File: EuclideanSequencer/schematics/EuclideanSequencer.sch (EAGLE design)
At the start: 46 parts, among them IC1 MEGA168, Q1 2N3904, Q2 2N3904, Q3 2N3904, Q4 2N3904, Y1 16Mhz

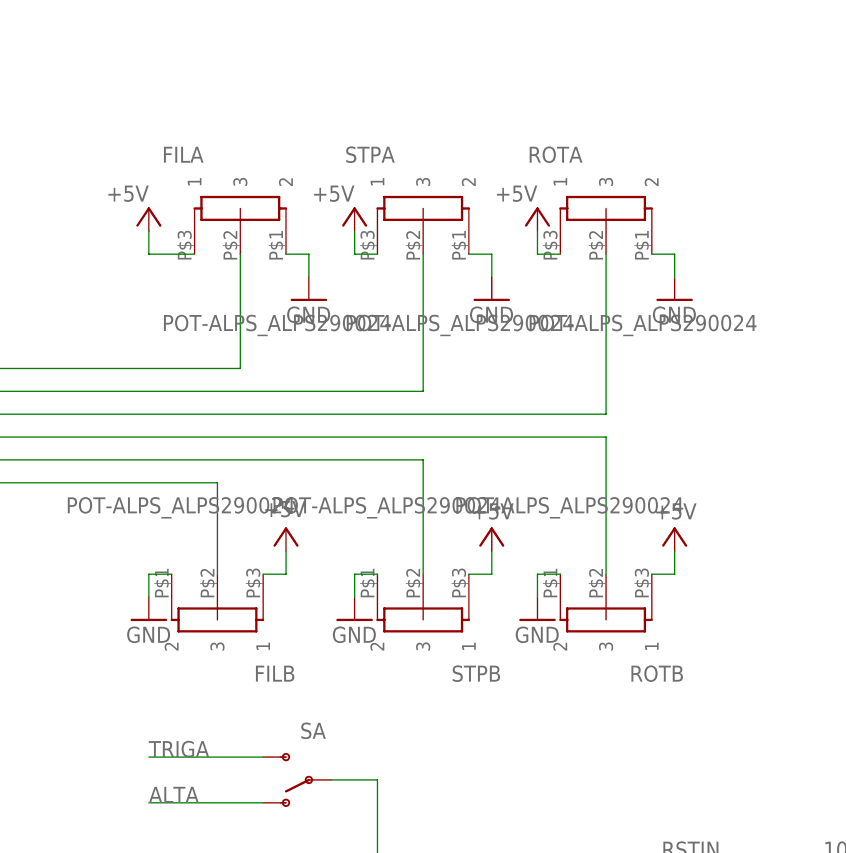
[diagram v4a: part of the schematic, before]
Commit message: moved pots around.
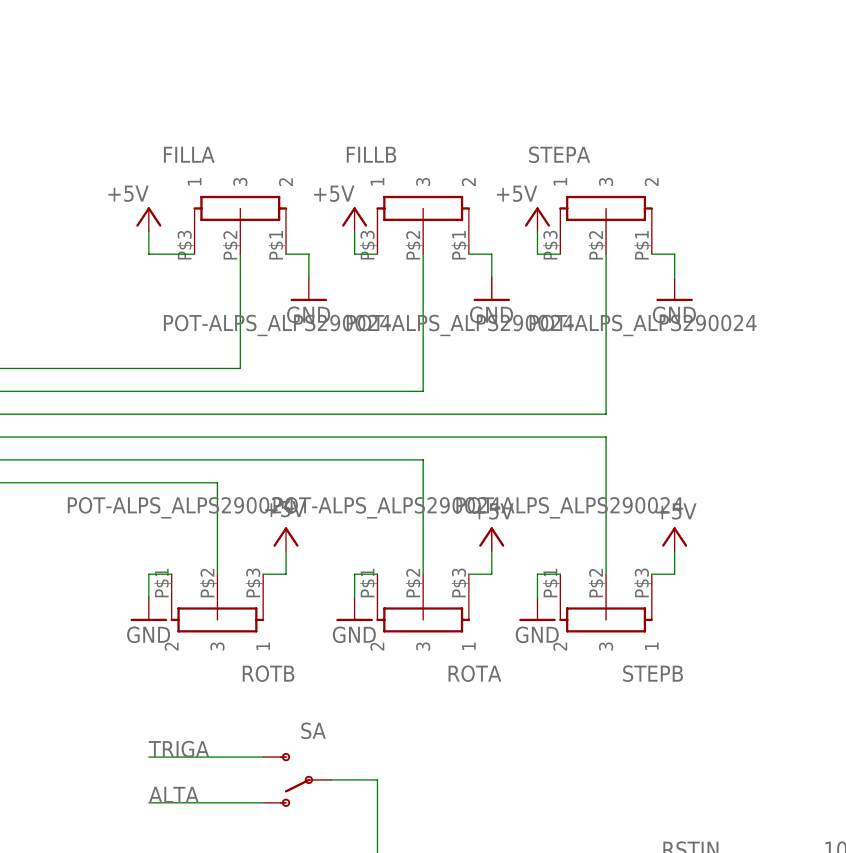
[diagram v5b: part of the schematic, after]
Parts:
- removed FILB, STPB: POT-ALPS_ALPS290024, Rebel:POT-ALPS_ALPS290024
- added STEPA, STEPB: POT-ALPS_ALPS290024, Rebel:POT-ALPS_ALPS290024
- renumbered FILA to FILLA, STPA to FILLB
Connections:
- net N$2 renamed FILFB
- net +5V: now also STEPA.1, STEPB.1; no longer FILB.1, STPB.1
- net GND: now also STEPA.2, STEPB.2; no longer FILB.2, STPB.2
- net N$3: now also STEPA.3; no longer ROTA.3
- net N$4: now also STEPB.3; no longer ROTB.3
- net N$5: now also ROTA.3; no longer STPB.3
- net N$6: now also ROTB.3; no longer FILB.3
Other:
- moved on the sheet: ROTA, ROTB
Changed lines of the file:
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@@
 <part name="CLKB" library="Rebel" deviceset="CON-LUMBERG_1502_03" device=""/>
 <part name="CLKTH" library="Rebel" deviceset="CON-LUMBERG_1502_03" device=""/>
-<part name="FILA" library="Rebel" deviceset="POT-ALPS_ALPS290024" device=""/>
-<part name="STPA" library="Rebel" deviceset="POT-ALPS_ALPS290024" device=""/>
+<part name="FILLA" library="Rebel" deviceset="POT-ALPS_ALPS290024" device=""/>
+<part name="FILLB" library="Rebel" deviceset="POT-ALPS_ALPS290024" device=""/>
+<part name="STEPA" library="Rebel" deviceset="POT-ALPS_ALPS290024" device=""/>
+<part name="ROTB" library="Rebel" deviceset="POT-ALPS_ALPS290024" device=""/>
 <part name="ROTA" library="Rebel" deviceset="POT-ALPS_ALPS290024" device=""/>
-<part name="FILB" library="Rebel" deviceset="POT-ALPS_ALPS290024" device=""/>
-<part name="STPB" library="Rebel" deviceset="POT-ALPS_ALPS290024" device=""/>
-<part name="ROTB" library="Rebel" deviceset="POT-ALPS_ALPS290024" device=""/>
+<part name="STEPB" library="Rebel" deviceset="POT-ALPS_ALPS290024" device=""/>
 <part name="CLKIN" library="Rebel" deviceset="CON-LUMBERG_1502_03" device=""/>
 <part name="RSTIN" library="Rebel" deviceset="CON-LUMBERG_1502_03" device=""/>
@@
 <instance part="CLKB" gate="G$1" x="144.78" y="-35.56"/>
 <instance part="CLKTH" gate="G$1" x="-7.62" y="-20.32" rot="MR0"/>
-<instance part="FILA" gate="G$1" x="139.7" y="91.44"/>
-<instance part="STPA" gate="G$1" x="160.02" y="91.44"/>
-<instance part="ROTA" gate="G$1" x="180.34" y="91.44"/>
-<instance part="FILB" gate="G$1" x="137.16" y="45.72" rot="R180"/>
-<instance part="STPB" gate="G$1" x="160.02" y="45.72" rot="R180"/>
-<instance part="ROTB" gate="G$1" x="180.34" y="45.72" rot="R180"/>
+<instance part="FILLA" gate="G$1" x="139.7" y="91.44"/>
+<instance part="FILLB" gate="G$1" x="160.02" y="91.44"/>
+<instance part="STEPA" gate="G$1" x="180.34" y="91.44"/>
+<instance part="ROTB" gate="G$1" x="137.16" y="45.72" rot="R180"/>
+<instance part="ROTA" gate="G$1" x="160.02" y="45.72" rot="R180"/>
+<instance part="STEPB" gate="G$1" x="180.34" y="45.72" rot="R180"/>
 <instance part="CLKIN" gate="G$1" x="-7.62" y="-43.18" rot="MR0"/>
 <instance part="RSTIN" gate="G$1" x="190.5" y="15.24" rot="MR0"/>
@@
 <wire x1="81.28" y1="73.66" x2="139.7" y2="73.66" width="0.1524" layer="91"/>
 <wire x1="139.7" y1="73.66" x2="139.7" y2="86.36" width="0.1524" layer="91"/>
-<pinref part="FILA" gate="G$1" pin="3"/>
-</segment>
-</net>
-<net name="N$2" class="0">
+<pinref part="FILLA" gate="G$1" pin="3"/>
+</segment>
+</net>
+<net name="FILFB" class="0">
 <segment>
 <pinref part="IC1" gate="G$1" pin="PC1(ADC1)"/>
 <wire x1="81.28" y1="71.12" x2="160.02" y2="71.12" width="0.1524" layer="91"/>
 <wire x1="160.02" y1="71.12" x2="160.02" y2="86.36" width="0.1524" layer="91"/>
-<pinref part="STPA" gate="G$1" pin="3"/>
+<pinref part="FILLB" gate="G$1" pin="3"/>
 </segment>
 </net>
@@
 <wire x1="81.28" y1="68.58" x2="180.34" y2="68.58" width="0.1524" layer="91"/>
 <wire x1="180.34" y1="68.58" x2="180.34" y2="86.36" width="0.1524" layer="91"/>
-<pinref part="ROTA" gate="G$1" pin="3"/>
+<pinref part="STEPA" gate="G$1" pin="3"/>
 </segment>
 </net>
@@
 <wire x1="81.28" y1="66.04" x2="180.34" y2="66.04" width="0.1524" layer="91"/>
 <wire x1="180.34" y1="66.04" x2="180.34" y2="50.8" width="0.1524" layer="91"/>
-<pinref part="ROTB" gate="G$1" pin="3"/>
+<pinref part="STEPB" gate="G$1" pin="3"/>
 </segment>
 </net>
@@
 <wire x1="81.28" y1="63.5" x2="160.02" y2="63.5" width="0.1524" layer="91"/>
 <wire x1="160.02" y1="63.5" x2="160.02" y2="50.8" width="0.1524" layer="91"/>
-<pinref part="STPB" gate="G$1" pin="3"/>
+<pinref part="ROTA" gate="G$1" pin="3"/>
 </segment>
 </net>
@@
 <pinref part="IC1" gate="G$1" pin="PC5(ADC5/SCL)"/>
 <wire x1="81.28" y1="60.96" x2="137.16" y2="60.96" width="0.1524" layer="91"/>
-<pinref part="FILB" gate="G$1" pin="3"/>
+<pinref part="ROTB" gate="G$1" pin="3"/>
 <wire x1="137.16" y1="50.8" x2="137.16" y2="60.96" width="0.1524" layer="91"/>
 </segment>
@@
 <pinref part="P+1" gate="1" pin="+5V"/>
 <wire x1="129.54" y1="88.9" x2="129.54" y2="86.36" width="0.1524" layer="91"/>
-<pinref part="FILA" gate="G$1" pin="1"/>
+<pinref part="FILLA" gate="G$1" pin="1"/>
 <wire x1="129.54" y1="86.36" x2="134.62" y2="86.36" width="0.1524" layer="91"/>
 </segment>
@@
 <pinref part="P+2" gate="1" pin="+5V"/>
 <wire x1="152.4" y1="88.9" x2="152.4" y2="86.36" width="0.1524" layer="91"/>
-<pinref part="STPA" gate="G$1" pin="1"/>
+<pinref part="FILLB" gate="G$1" pin="1"/>
 <wire x1="152.4" y1="86.36" x2="154.94" y2="86.36" width="0.1524" layer="91"/>
 </segment>
@@
 <pinref part="P+3" gate="1" pin="+5V"/>
 <wire x1="172.72" y1="88.9" x2="172.72" y2="86.36" width="0.1524" layer="91"/>
-<pinref part="ROTA" gate="G$1" pin="1"/>
+<pinref part="STEPA" gate="G$1" pin="1"/>
 <wire x1="175.26" y1="86.36" x2="172.72" y2="86.36" width="0.1524" layer="91"/>
 </segment>
@@
 <pinref part="P+6" gate="1" pin="+5V"/>
 <wire x1="187.96" y1="53.34" x2="187.96" y2="50.8" width="0.1524" layer="91"/>
-<pinref part="ROTB" gate="G$1" pin="1"/>
+<pinref part="STEPB" gate="G$1" pin="1"/>
 <wire x1="187.96" y1="50.8" x2="185.42" y2="50.8" width="0.1524" layer="91"/>
 </segment>
@@
 <pinref part="P+5" gate="1" pin="+5V"/>
 <wire x1="167.64" y1="53.34" x2="167.64" y2="50.8" width="0.1524" layer="91"/>
-<pinref part="STPB" gate="G$1" pin="1"/>
+<pinref part="ROTA" gate="G$1" pin="1"/>
 <wire x1="167.64" y1="50.8" x2="165.1" y2="50.8" width="0.1524" layer="91"/>
 </segment>
@@
 <pinref part="P+4" gate="1" pin="+5V"/>
 <wire x1="144.78" y1="53.34" x2="144.78" y2="50.8" width="0.1524" layer="91"/>
-<pinref part="FILB" gate="G$1" pin="1"/>
+<pinref part="ROTB" gate="G$1" pin="1"/>
 <wire x1="142.24" y1="50.8" x2="144.78" y2="50.8" width="0.1524" layer="91"/>
 </segment>
@@
 <pinref part="GND1" gate="1" pin="GND"/>
 <wire x1="129.54" y1="48.26" x2="129.54" y2="50.8" width="0.1524" layer="91"/>
-<pinref part="FILB" gate="G$1" pin="2"/>
+<pinref part="ROTB" gate="G$1" pin="2"/>
 <wire x1="132.08" y1="50.8" x2="129.54" y2="50.8" width="0.1524" layer="91"/>
 </segment>
@@
 <pinref part="GND2" gate="1" pin="GND"/>
 <wire x1="152.4" y1="48.26" x2="152.4" y2="50.8" width="0.1524" layer="91"/>
-<pinref part="STPB" gate="G$1" pin="2"/>
+<pinref part="ROTA" gate="G$1" pin="2"/>
 <wire x1="154.94" y1="50.8" x2="152.4" y2="50.8" width="0.1524" layer="91"/>
 </segment>
@@
 <pinref part="GND3" gate="1" pin="GND"/>
 <wire x1="172.72" y1="48.26" x2="172.72" y2="50.8" width="0.1524" layer="91"/>
-<pinref part="ROTB" gate="G$1" pin="2"/>
+<pinref part="STEPB" gate="G$1" pin="2"/>
 <wire x1="172.72" y1="50.8" x2="175.26" y2="50.8" width="0.1524" layer="91"/>
 </segment>
@@
 <pinref part="GND6" gate="1" pin="GND"/>
 <wire x1="147.32" y1="86.36" x2="147.32" y2="83.82" width="0.1524" layer="91"/>
-<pinref part="FILA" gate="G$1" pin="2"/>
+<pinref part="FILLA" gate="G$1" pin="2"/>
 <wire x1="147.32" y1="86.36" x2="144.78" y2="86.36" width="0.1524" layer="91"/>
 </segment>
@@
 <pinref part="GND5" gate="1" pin="GND"/>
 <wire x1="167.64" y1="86.36" x2="167.64" y2="83.82" width="0.1524" layer="91"/>
-<pinref part="STPA" gate="G$1" pin="2"/>
+<pinref part="FILLB" gate="G$1" pin="2"/>
 <wire x1="167.64" y1="86.36" x2="165.1" y2="86.36" width="0.1524" layer="91"/>
 </segment>
@@
 <pinref part="GND4" gate="1" pin="GND"/>
 <wire x1="187.96" y1="86.36" x2="187.96" y2="83.82" width="0.1524" layer="91"/>
-<pinref part="ROTA" gate="G$1" pin="2"/>
+<pinref part="STEPA" gate="G$1" pin="2"/>
 <wire x1="185.42" y1="86.36" x2="187.96" y2="86.36" width="0.1524" layer="91"/>
 </segment>

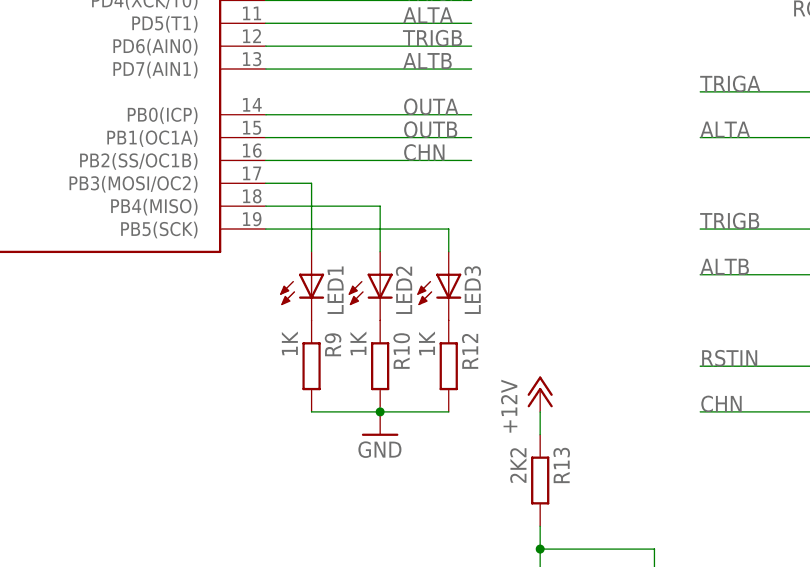
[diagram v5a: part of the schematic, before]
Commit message: reorganised board layout
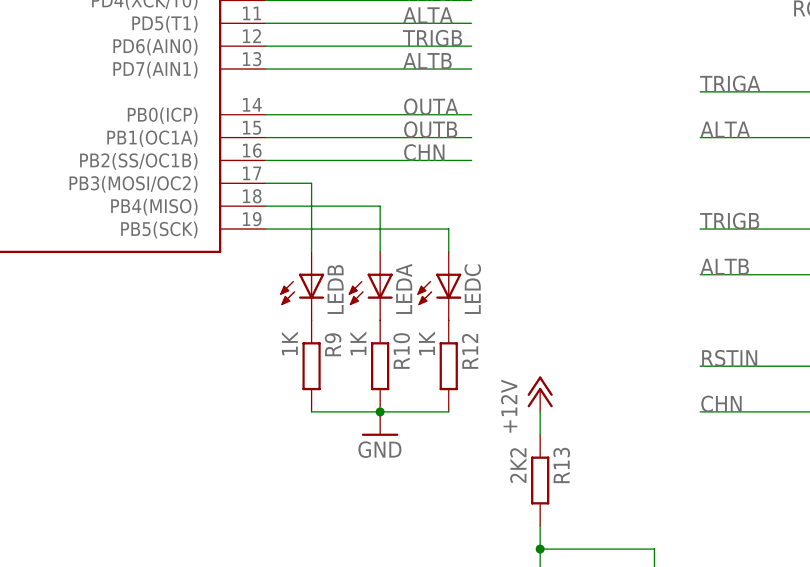
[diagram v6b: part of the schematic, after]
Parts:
- renumbered LED1 to LEDB, LED2 to LEDA, LED3 to LEDC
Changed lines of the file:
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@@
 <part name="P+15" library="supply1" deviceset="+5V" device=""/>
 <part name="SC" library="SparkFun" deviceset="SWITCH-SPST" device="PTH"/>
-<part name="LED1" library="SparkFun" deviceset="LED" device="3MM"/>
-<part name="LED2" library="SparkFun" deviceset="LED" device="3MM"/>
-<part name="LED3" library="SparkFun" deviceset="LED" device="3MM"/>
+<part name="LEDB" library="SparkFun" deviceset="LED" device="3MM"/>
+<part name="LEDA" library="SparkFun" deviceset="LED" device="3MM"/>
+<part name="LEDC" library="SparkFun" deviceset="LED" device="3MM"/>
 <part name="R9" library="rcl" deviceset="R-EU_" device="0204/7" value="1K"/>
 <part name="R10" library="rcl" deviceset="R-EU_" device="0204/7" value="1K"/>
@@
 <instance part="P+15" gate="1" x="15.24" y="99.06"/>
 <instance part="SC" gate="1" x="147.32" y="-2.54" rot="R180"/>
-<instance part="LED1" gate="G$1" x="86.36" y="10.16"/>
-<instance part="LED2" gate="G$1" x="93.98" y="10.16"/>
-<instance part="LED3" gate="G$1" x="101.6" y="10.16"/>
+<instance part="LEDB" gate="G$1" x="86.36" y="10.16"/>
+<instance part="LEDA" gate="G$1" x="93.98" y="10.16"/>
+<instance part="LEDC" gate="G$1" x="101.6" y="10.16"/>
 <instance part="R9" gate="G$1" x="86.36" y="0" rot="R270"/>
 <instance part="R10" gate="G$1" x="93.98" y="0" rot="R270"/>
@@
 <segment>
 <pinref part="IC1" gate="G$1" pin="PB4(MISO)"/>
-<pinref part="LED2" gate="G$1" pin="A"/>
+<pinref part="LEDA" gate="G$1" pin="A"/>
 <wire x1="93.98" y1="17.78" x2="81.28" y2="17.78" width="0.1524" layer="91"/>
 <wire x1="93.98" y1="12.7" x2="93.98" y2="17.78" width="0.1524" layer="91"/>
@@
 <pinref part="IC1" gate="G$1" pin="PB5(SCK)"/>
 <wire x1="81.28" y1="15.24" x2="101.6" y2="15.24" width="0.1524" layer="91"/>
-<pinref part="LED3" gate="G$1" pin="A"/>
+<pinref part="LEDC" gate="G$1" pin="A"/>
 <wire x1="101.6" y1="12.7" x2="101.6" y2="15.24" width="0.1524" layer="91"/>
 </segment>
@@
 <net name="N$24" class="0">
 <segment>
-<pinref part="LED1" gate="G$1" pin="C"/>
+<pinref part="LEDB" gate="G$1" pin="C"/>
 <pinref part="R9" gate="G$1" pin="1"/>
 </segment>
@@
 <net name="N$28" class="0">
 <segment>
-<pinref part="LED2" gate="G$1" pin="C"/>
+<pinref part="LEDA" gate="G$1" pin="C"/>
 <pinref part="R10" gate="G$1" pin="1"/>
 </segment>
@@
 <net name="N$30" class="0">
 <segment>
-<pinref part="LED3" gate="G$1" pin="C"/>
+<pinref part="LEDC" gate="G$1" pin="C"/>
 <pinref part="R12" gate="G$1" pin="1"/>
 </segment>
@@
 <segment>
 <pinref part="IC1" gate="G$1" pin="PB3(MOSI/OC2)"/>
-<pinref part="LED1" gate="G$1" pin="A"/>
+<pinref part="LEDB" gate="G$1" pin="A"/>
 <wire x1="81.28" y1="20.32" x2="86.36" y2="20.32" width="0.1524" layer="91"/>
 <wire x1="86.36" y1="20.32" x2="86.36" y2="12.7" width="0.1524" layer="91"/>

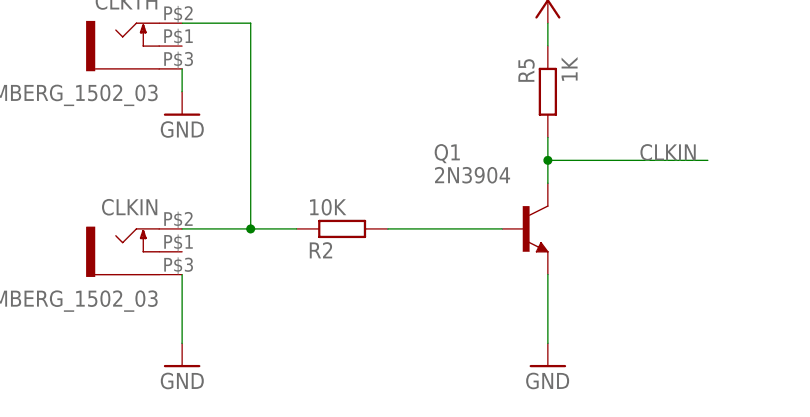
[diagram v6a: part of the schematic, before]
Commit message: worked out some resistors
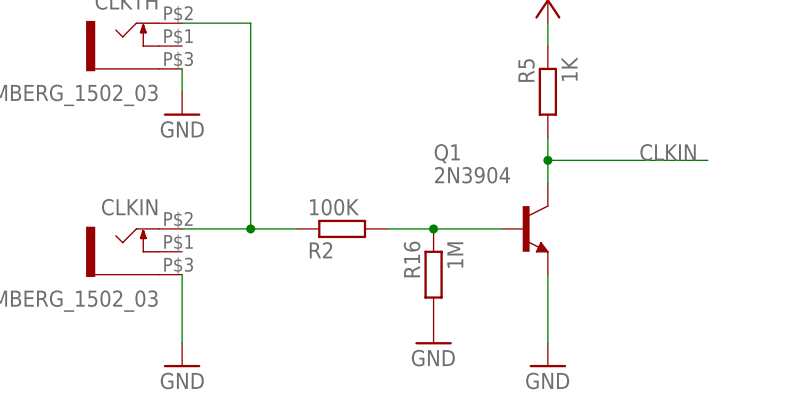
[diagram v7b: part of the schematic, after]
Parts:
- added R16: 1M, rcl:R-EU_0204/7
- R2: value 10K -> 100K
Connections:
- net GND: now also R16.2
- net N$17: now also R16.1
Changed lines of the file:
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@@
 <?xml version="1.0" encoding="utf-8"?>
 <!DOCTYPE eagle SYSTEM "eagle.dtd">
-<eagle version="6.1">
+<eagle version="6.0">
 <drawing>
 <settings>
@@
 <part name="C3" library="rcl" deviceset="C-US" device="050-024X044" value="100n"/>
 <part name="GND9" library="supply1" deviceset="GND" device=""/>
-<part name="R2" library="rcl" deviceset="R-EU_" device="0204/7" value="10K"/>
+<part name="R2" library="rcl" deviceset="R-EU_" device="0204/7" value="100K"/>
 <part name="SA" library="SparkFun" deviceset="SWITCH-SPST" device="KIT"/>
 <part name="GND12" library="supply1" deviceset="GND" device=""/>
@@
 <part name="P+16" library="supply1" deviceset="+5V" device=""/>
 <part name="U$2" library="SparkFun" deviceset="M08X2" device=""/>
+<part name="R16" library="rcl" deviceset="R-EU_" device="0204/7" value="1M"/>
+<part name="GND8" library="supply1" deviceset="GND" device=""/>
 </parts>
 <sheets>
@@
 </instance>
 <instance part="U$2" gate="G$1" x="236.22" y="73.66" rot="R180"/>
+<instance part="R16" gate="G$1" x="25.4" y="-45.72" rot="MR270"/>
+<instance part="GND8" gate="1" x="25.4" y="-53.34"/>
 </instances>
 <busses>
@@
 <junction x="198.12" y="12.7"/>
 </segment>
+<segment>
+<pinref part="R16" gate="G$1" pin="2"/>
+<pinref part="GND8" gate="1" pin="GND"/>
+</segment>
 </net>
 <net name="N$9" class="0">
@@
 <segment>
 <pinref part="R2" gate="G$1" pin="2"/>
-<wire x1="33.02" y1="-40.64" x2="20.32" y2="-40.64" width="0.1524" layer="91"/>
+<wire x1="33.02" y1="-40.64" x2="25.4" y2="-40.64" width="0.1524" layer="91"/>
 <pinref part="Q1" gate="G1" pin="B"/>
-</segment>
-</net>
+<pinref part="R16" gate="G$1" pin="1"/>
+<wire x1="25.4" y1="-40.64" x2="20.32" y2="-40.64" width="0.1524" layer="91"/>
+<junction x="25.4" y="-40.64"/>
+</segment>
+</net>
